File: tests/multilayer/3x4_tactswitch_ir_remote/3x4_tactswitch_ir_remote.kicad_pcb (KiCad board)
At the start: 2 copper layers, 34.3 x 48.3 mm, 21 parts, among them J2 Conn_01x06_Pin, SW1 SW_Push, SW10 SW_Push, SW11 SW_Push, SW12 SW_Push, SW2 SW_Push, SW3 SW_Push, SW4 SW_Push, SW5 SW_Push, SW6 SW_Push, SW7 SW_Push, SW8 SW_Push, SW9 SW_Push, U1 ATmega328P-AU, Y1 Crystal_GND23

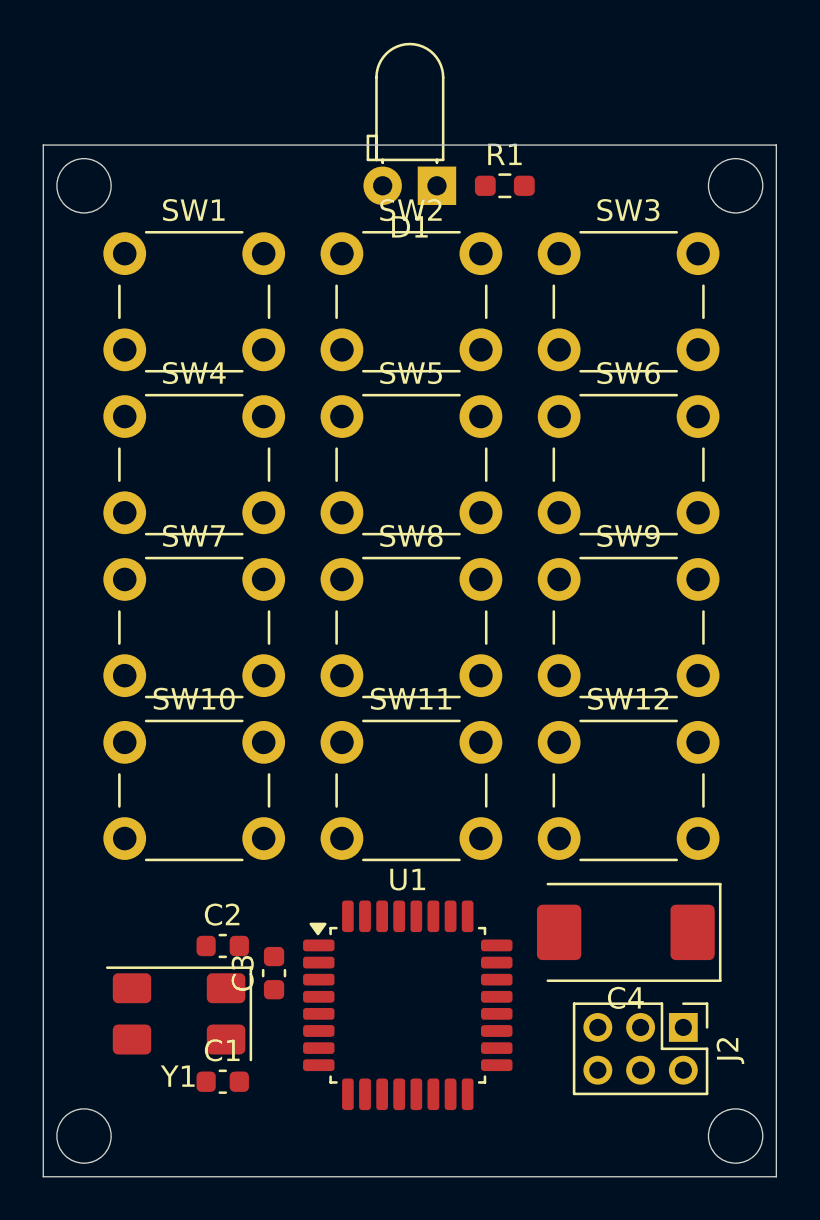
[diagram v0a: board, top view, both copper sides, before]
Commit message: chore: Increase board north outline margin in 3x4_tactswitch_ir_remote screenshot and project
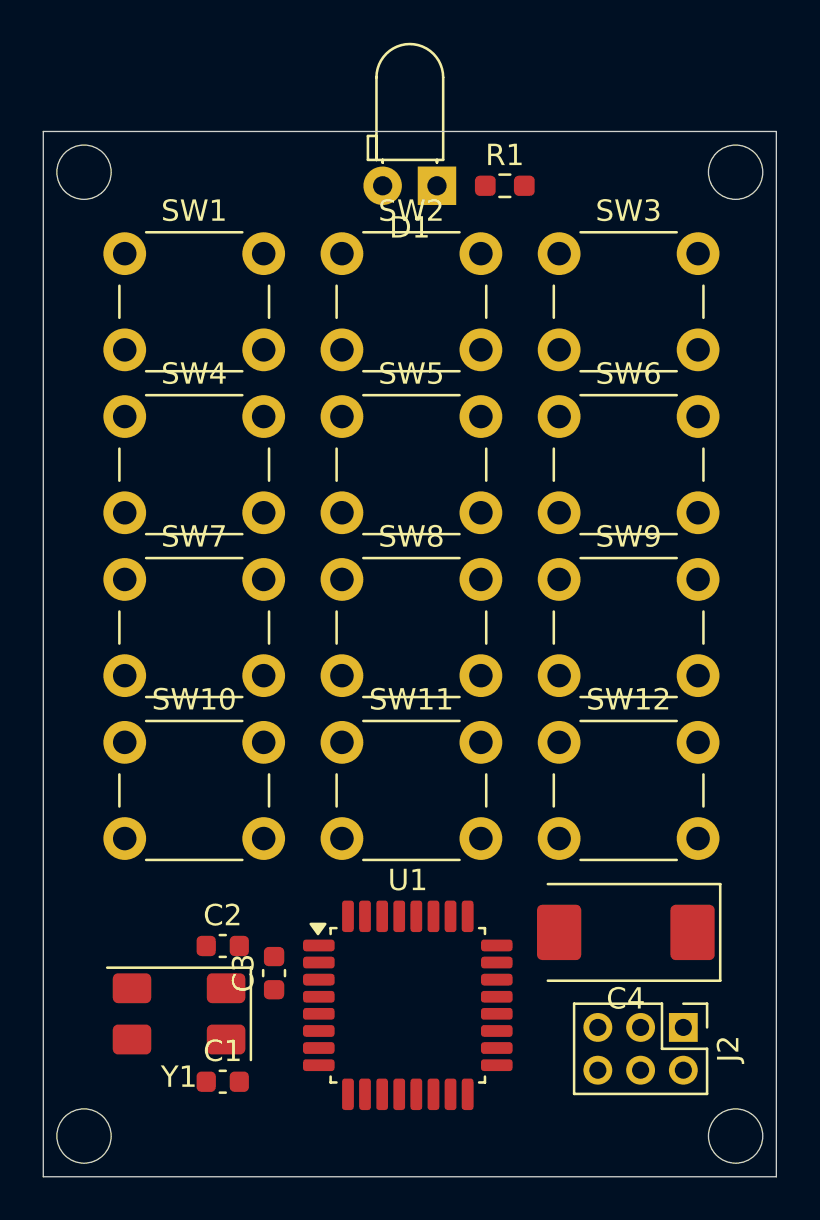
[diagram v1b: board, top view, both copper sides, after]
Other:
- board size 34.3 x 48.3 mm -> 34.3 x 48.9 mm
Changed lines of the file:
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@@
 			(at 3.75 6.7 0)
 			(layer "F.Fab")
+			(hide yes)
 			(effects
 				(font
@@
 			(at 3.75 6.7 0)
 			(layer "F.Fab")
+			(hide yes)
 			(effects
 				(font
@@
 			(at 3.75 6.7 0)
 			(layer "F.Fab")
+			(hide yes)
 			(effects
 				(font
@@
 			(at 3.75 6.7 0)
 			(layer "F.Fab")
+			(hide yes)
 			(effects
 				(font
@@
 			(at 3.75 6.7 0)
 			(layer "F.Fab")
+			(hide yes)
 			(effects
 				(font
@@
 			(at 0 1.43 90)
 			(layer "F.Fab")
+			(hide yes)
 			(effects
 				(font
@@
 			(at 3.75 6.7 0)
 			(layer "F.Fab")
+			(hide yes)
 			(effects
 				(font
@@
 			(at 0 1.43 0)
 			(layer "F.Fab")
+			(hide yes)
 			(effects
 				(font
@@
 			(at 3.75 6.7 0)
 			(layer "F.Fab")
+			(hide yes)
 			(effects
 				(font
@@
 			(at 0 2.95 0)
 			(layer "F.Fab")
+			(hide yes)
 			(effects
 				(font
@@
 			(at 1 6.11 90)
 			(layer "F.Fab")
+			(hide yes)
 			(effects
 				(font
@@
 		)
 		(fp_text user "${REFERENCE}"
-			(at 1 2 0)
+			(at 3.81 2 0)
 			(layer "F.Fab")
 			(effects
@@
 			(at 0 1.43 0)
 			(layer "F.Fab")
+			(hide yes)
 			(effects
 				(font
@@
 			(at 3.75 6.7 0)
 			(layer "F.Fab")
+			(hide yes)
 			(effects
 				(font
@@
 			(at 3.75 6.7 0)
 			(layer "F.Fab")
+			(hide yes)
 			(effects
 				(font
@@
 			(at 3.75 6.7 0)
 			(layer "F.Fab")
+			(hide yes)
 			(effects
 				(font
@@
 			(at 0 3.1 0)
 			(layer "F.Fab")
+			(hide yes)
 			(effects
 				(font
@@
 			(at 3.75 6.7 0)
 			(layer "F.Fab")
+			(hide yes)
 			(effects
 				(font
@@
 			(at 0 5.85 0)
 			(layer "F.Fab")
+			(hide yes)
 			(effects
 				(font
@@
 			(at 3.75 6.7 0)
 			(layer "F.Fab")
+			(hide yes)
 			(effects
 				(font
@@
 			(at 0 1.43 0)
 			(layer "F.Fab")
+			(hide yes)
 			(effects
 				(font
@@
 	)
 	(gr_circle
-		(center 142.875 65.405)
-		(end 144.145 65.405)
+		(center 142.875 64.77)
+		(end 144.145 64.77)
 		(stroke
 			(width 0.05)
@@
 	)
 	(gr_circle
-		(center 173.355 65.405)
-		(end 174.625 65.405)
+		(center 173.355 64.77)
+		(end 174.625 64.77)
 		(stroke
 			(width 0.05)
@@
 	)
 	(gr_rect
-		(start 140.97 63.5)
+		(start 140.97 62.865)
 		(end 175.26 111.76)
 		(stroke
